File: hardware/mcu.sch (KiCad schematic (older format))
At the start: 23 parts, among them P3 SWD, P4 SPI3, P5 UART5, P7 USB_B, SW1 RESET, SW2 BOOT, U5 STM32F405R, U7 USBUF01W6, X1 8MHz

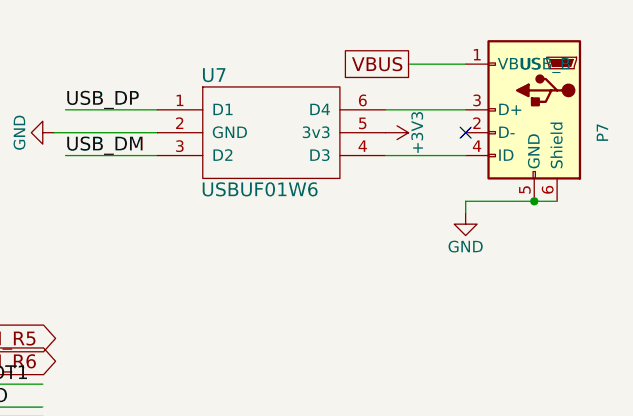
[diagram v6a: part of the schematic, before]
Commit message: Disconnect pullup from USBUF
STM32 has internal pullups
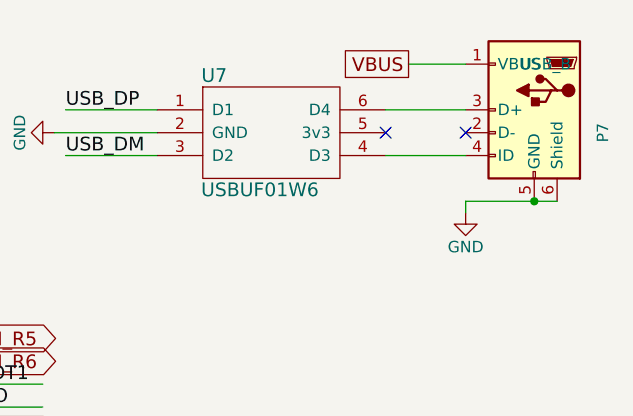
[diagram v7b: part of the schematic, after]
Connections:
- net labels removed: +3V3
- no-connect marks 3 -> 4
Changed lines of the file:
@@
 	1    0    0    -1
-$EndComp
-$Comp
-L +3V3 #PWR034
-U 1 1 582B948D
-P 10100 1050
-F 0 "#PWR034" H 10100 900 50  0001 C CNN
-F 1 "+3V3" H 10100 1190 50  0000 C CNN
-F 2 "" H 10100 1050 50  0000 C CNN
-F 3 "" H 10100 1050 50  0000 C CNN
-	1    10100 1050
-	0    1    1    0
 $EndComp
 Text GLabel 10200 750  0    60   UnSpc ~ 0
@@
 	10450 1350 10850 1350
 Connection ~ 10750 1350
+NoConn ~ 10100 1050
 $EndSCHEMATC

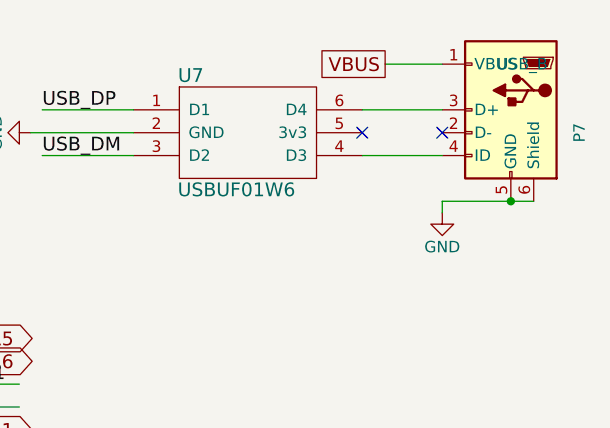
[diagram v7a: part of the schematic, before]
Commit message: PCB fixes for 1.1
* Disconnect DATA lines in daisy chain
* Fix barrel jack footprint (hole size)
* Fix some 3D models
* Update PCB netlist
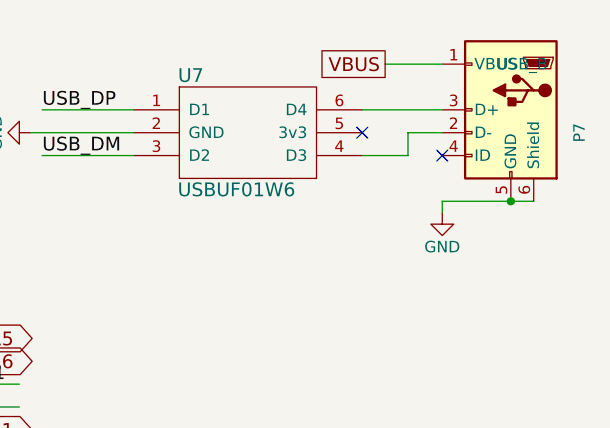
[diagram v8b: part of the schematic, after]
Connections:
- wire segments 59 -> 61
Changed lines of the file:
@@
 Text GLabel 10200 750  0    60   UnSpc ~ 0
 VBUS
-NoConn ~ 10450 1050
 $Comp
 L C C22
@@
 $EndComp
 $Comp
-L GND #PWR035
+L GND #PWR034
 U 1 1 58784915
 P 3900 950
-F 0 "#PWR035" H 3900 700 50  0001 C CNN
+F 0 "#PWR034" H 3900 700 50  0001 C CNN
 F 1 "GND" H 3900 800 50  0000 C CNN
 F 2 "" H 3900 950 50  0000 C CNN
@@
 	10100 950  10450 950
 Wire Wire Line
-	10100 1150 10450 1150
-Wire Wire Line
 	8650 1050 9100 1050
 Wire Wire Line
@@
 Connection ~ 10750 1350
 NoConn ~ 10100 1050
+Wire Wire Line
+	10100 1150 10300 1150
+Wire Wire Line
+	10300 1150 10300 1050
+Wire Wire Line
+	10300 1050 10450 1050
+NoConn ~ 10450 1150
 $EndSCHEMATC
